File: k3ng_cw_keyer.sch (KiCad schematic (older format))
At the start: 51 parts, among them J1 Jack-DC, J2 Conn_01x06, J3 Conn_01x03, J4 Conn_01x04, J5 Mini-DIN-6, J6 Audio-Jack-3, J7 Audio-Jack-3, J8 Audio-Jack-3, Q1 Q_NPN_BCE, SW1 SW_Push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

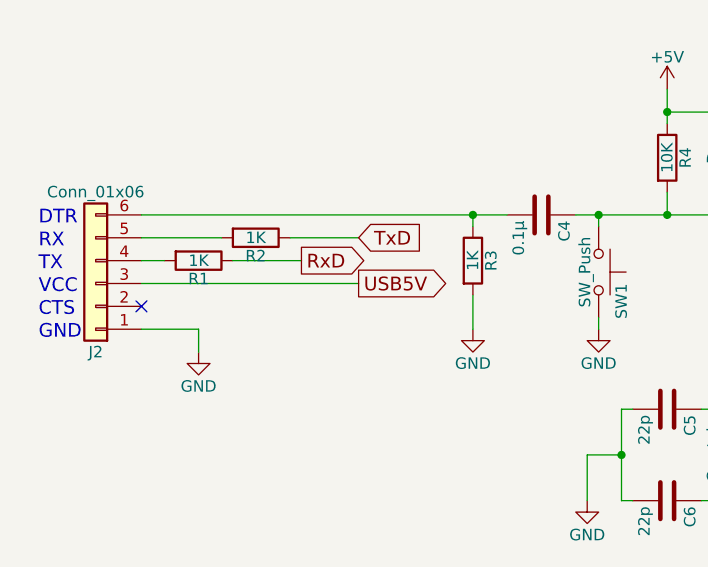
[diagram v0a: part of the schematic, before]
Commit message: del USB5V
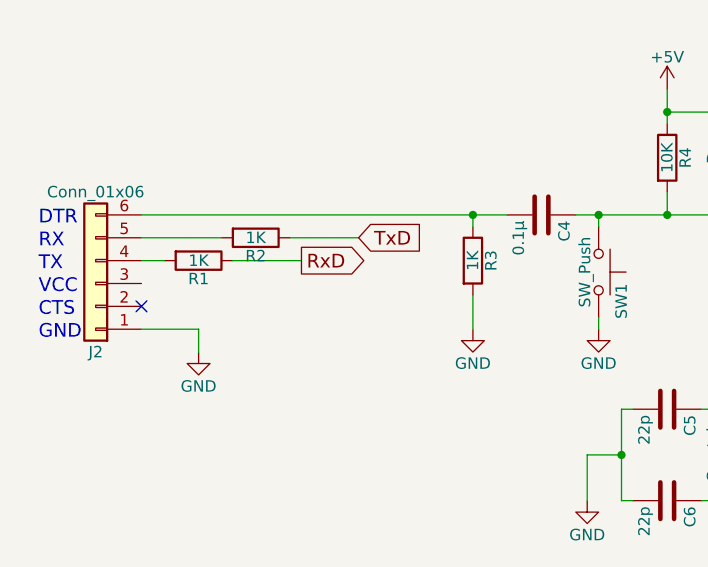
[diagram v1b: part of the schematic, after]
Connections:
- wire segments 170 -> 169
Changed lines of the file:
@@
 Text GLabel 3550 5700 3    60   Input ~ 0
-USB5V
-Text GLabel 2550 2450 2    60   Output ~ 0
 USB5V
 Wire Wire Line
@@
 	2000 2350 2300 2350
 Wire Wire Line
-	2550 2450 1600 2450
-Wire Wire Line
 	1850 2650 1600 2650

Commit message: Update POT
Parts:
- RV1: value POT -> 10K
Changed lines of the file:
@@
 P 6750 1950
 F 0 "RV1" V 6575 1950 50  0000 C CNN
-F 1 "POT" V 6650 1950 50  0000 C CNN
+F 1 "10K" V 6650 1950 50  0000 C CNN
 F 2 "" H 6750 1950 50  0001 C CNN
 F 3 "" H 6750 1950 50  0001 C CNN

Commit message: Update
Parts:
- removed J6, J7, J8: Audio-Jack-3, Connectors_JST:JST_ZE_S03B-ZESK-2D_03x1.5mm_Angled, symbol Audio-Jack-3
- added J6, J7, J8: AJ-1780, symbol AJ-1780
- RV1: value 10K -> POT
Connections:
- wire segments 169 -> 136
- no-connect marks 24 -> 30
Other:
- moved on the sheet: C13, J4, R7, U3B
